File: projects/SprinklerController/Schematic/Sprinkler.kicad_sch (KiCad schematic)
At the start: 37 parts

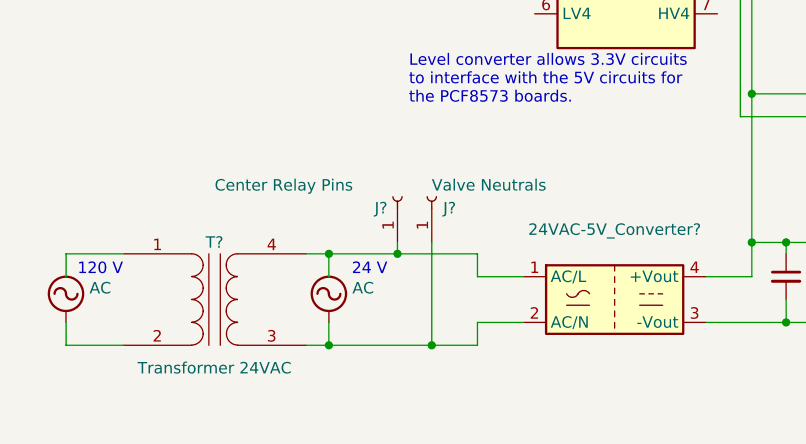
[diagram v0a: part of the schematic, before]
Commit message: Minor correction to schematic
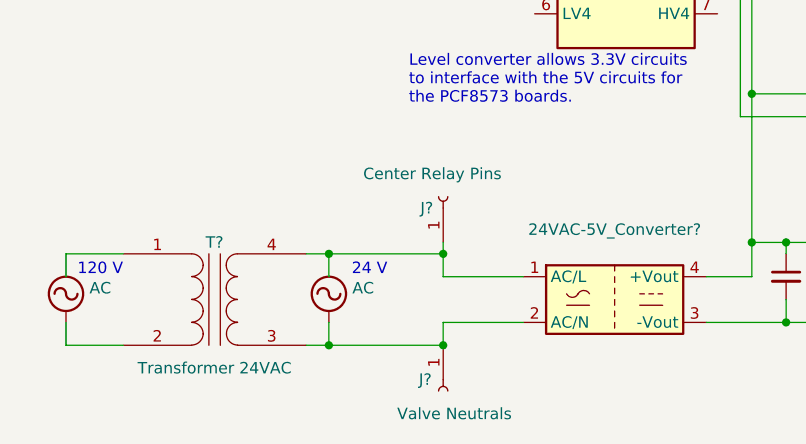
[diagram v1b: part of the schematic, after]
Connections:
- net at U?.3 (P2): no longer U?.3 (P2)
- net at U?.4 (VCC): no longer U?.4 (VCC)
- net at U?.1 (SCL): now also U?.1 (SCL)
- net at U?.1 (SCL): no longer U?.1 (SCL)
- net at U?.2 (SDA): now also U?.2 (SDA)
- net at U?.2 (SDA): no longer U?.2 (SDA)
- net at U?.3 (P2): now also U?.3 (P2)
- net at U?.4 (VCC): now also U?.4 (VCC)
- new net: U?.3 (P2), U?.3 (P2)
- new net: U?.4 (VCC), U?.4 (VCC)
- now unconnected: U?.3 (P2), U?.4 (VCC)
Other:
- moved on the sheet: J?
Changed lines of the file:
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@@
   (junction (at 246.38 104.14) (diameter 0) (color 0 0 0 0)
   )
+  (junction (at 66.04 184.15) (diameter 0) (color 0 0 0 0)
+  )
   (junction (at 166.37 104.14) (diameter 0) (color 0 0 0 0)
   )
@@
   (junction (at 199.39 59.69) (diameter 0) (color 0 0 0 0)
   )
-  (junction (at 60.96 173.99) (diameter 0) (color 0 0 0 0)
-  )
   (junction (at 54.61 137.16) (diameter 0) (color 0 0 0 0)
   )
@@
   (junction (at 240.03 129.54) (diameter 0) (color 0 0 0 0)
   )
-  (junction (at 64.77 184.15) (diameter 0) (color 0 0 0 0)
+  (junction (at 66.04 173.99) (diameter 0) (color 0 0 0 0)
   )
   (junction (at 246.38 92.71) (diameter 0) (color 0 0 0 0)
@@
     (stroke (width 0) (type default) (color 0 0 0 0))
   )
-  (wire (pts (xy 64.77 184.15) (xy 69.85 184.15))
+  (wire (pts (xy 53.34 184.15) (xy 66.04 184.15))
     (stroke (width 0) (type default) (color 0 0 0 0))
   )
@@
     (stroke (width 0) (type default) (color 0 0 0 0))
   )
-  (wire (pts (xy 69.85 184.15) (xy 69.85 181.61))
-    (stroke (width 0) (type default) (color 0 0 0 0))
-  )
-  (wire (pts (xy 60.96 173.99) (xy 69.85 173.99))
-    (stroke (width 0) (type default) (color 0 0 0 0))
-  )
   (wire (pts (xy 157.48 100.33) (xy 180.34 100.33))
     (stroke (width 0) (type default) (color 0 0 0 0))
@@
     (stroke (width 0) (type default) (color 0 0 0 0))
   )
+  (wire (pts (xy 74.93 176.53) (xy 66.04 176.53))
+    (stroke (width 0) (type default) (color 0 0 0 0))
+  )
   (wire (pts (xy 204.47 134.62) (xy 198.12 134.62))
     (stroke (width 0) (type default) (color 0 0 0 0))
@@
     (stroke (width 0) (type default) (color 0 0 0 0))
   )
+  (wire (pts (xy 66.04 181.61) (xy 66.04 184.15))
+    (stroke (width 0) (type default) (color 0 0 0 0))
+  )
   (wire (pts (xy 207.01 92.71) (xy 207.01 104.14))
     (stroke (width 0) (type default) (color 0 0 0 0))
@@
     (stroke (width 0) (type default) (color 0 0 0 0))
   )
+  (wire (pts (xy 66.04 172.72) (xy 66.04 173.99))
+    (stroke (width 0) (type default) (color 0 0 0 0))
+  )
   (wire (pts (xy 279.4 46.99) (xy 279.4 59.69))
     (stroke (width 0) (type default) (color 0 0 0 0))
@@
     (stroke (width 0) (type default) (color 0 0 0 0))
   )
-  (wire (pts (xy 60.96 172.72) (xy 60.96 173.99))
-    (stroke (width 0) (type default) (color 0 0 0 0))
-  )
   (wire (pts (xy 279.4 72.39) (xy 279.4 83.82))
     (stroke (width 0) (type default) (color 0 0 0 0))
@@
     (stroke (width 0) (type default) (color 0 0 0 0))
   )
-  (wire (pts (xy 69.85 176.53) (xy 74.93 176.53))
-    (stroke (width 0) (type default) (color 0 0 0 0))
-  )
   (wire (pts (xy 53.34 173.99) (xy 53.34 176.53))
     (stroke (width 0) (type default) (color 0 0 0 0))
@@
     (stroke (width 0) (type default) (color 0 0 0 0))
   )
+  (wire (pts (xy 66.04 176.53) (xy 66.04 173.99))
+    (stroke (width 0) (type default) (color 0 0 0 0))
+  )
   (wire (pts (xy 158.75 111.76) (xy 180.34 111.76))
     (stroke (width 0) (type default) (color 0 0 0 0))
@@
     (stroke (width 0) (type default) (color 0 0 0 0))
   )
-  (wire (pts (xy 53.34 184.15) (xy 64.77 184.15))
-    (stroke (width 0) (type default) (color 0 0 0 0))
-  )
   (wire (pts (xy 34.29 34.29) (xy 34.29 63.5))
     (stroke (width 0) (type default) (color 0 0 0 0))
@@
     (stroke (width 0) (type default) (color 0 0 0 0))
   )
-  (wire (pts (xy 69.85 173.99) (xy 69.85 176.53))
-    (stroke (width 0) (type default) (color 0 0 0 0))
-  )
   (wire (pts (xy 160.02 123.19) (xy 180.34 123.19))
     (stroke (width 0) (type default) (color 0 0 0 0))
@@
     (stroke (width 0) (type default) (color 0 0 0 0))
   )
-  (wire (pts (xy 69.85 181.61) (xy 74.93 181.61))
-    (stroke (width 0) (type default) (color 0 0 0 0))
-  )
   (wire (pts (xy 199.39 72.39) (xy 199.39 83.82))
     (stroke (width 0) (type default) (color 0 0 0 0))
@@
     (stroke (width 0) (type default) (color 0 0 0 0))
   )
-  (wire (pts (xy 64.77 172.72) (xy 64.77 184.15))
-    (stroke (width 0) (type default) (color 0 0 0 0))
-  )
   (wire (pts (xy 180.34 104.14) (xy 166.37 104.14))
     (stroke (width 0) (type default) (color 0 0 0 0))
@@
     (stroke (width 0) (type default) (color 0 0 0 0))
   )
-  (wire (pts (xy 53.34 173.99) (xy 60.96 173.99))
+  (wire (pts (xy 53.34 173.99) (xy 66.04 173.99))
     (stroke (width 0) (type default) (color 0 0 0 0))
   )
@@
   )
   (wire (pts (xy 24.13 184.15) (xy 30.48 184.15))
+    (stroke (width 0) (type default) (color 0 0 0 0))
+  )
+  (wire (pts (xy 74.93 181.61) (xy 66.04 181.61))
     (stroke (width 0) (type default) (color 0 0 0 0))
   )
@@
     (pin "5")
   )
-  (symbol (lib_id "Connector:Conn_01x01_Female") (at 60.96 167.64 90) (unit 1)
+  (symbol (lib_id "Connector:Conn_01x01_Female") (at 66.04 167.64 90) (unit 1)
     (in_bom yes) (on_board yes)
-    (property "Reference" "J?" (id 0) (at 58.42 168.91 90)
+    (property "Reference" "J?" (id 0) (at 63.5 168.91 90)
       (effects (font (size 1.27 1.27)) (justify right))
     )
-    (property "Value" "Center Relay Pins" (id 1) (at 40.64 166.37 90)
+    (property "Value" "Center Relay Pins" (id 1) (at 57.15 165.1 90)
       (effects (font (size 1.27 1.27)) (justify right))
     )
-    (property "Footprint" "" (id 2) (at 60.96 167.64 0)
-      (effects (font (size 1.27 1.27)) hide)
-    )
-    (property "Datasheet" "~" (id 3) (at 60.96 167.64 0)
+    (property "Footprint" "" (id 2) (at 66.04 167.64 0)
+      (effects (font (size 1.27 1.27)) hide)
+    )
+    (property "Datasheet" "~" (id 3) (at 66.04 167.64 0)
       (effects (font (size 1.27 1.27)) hide)
     )
@@
     (pin "9")
   )
-  (symbol (lib_id "Connector:Conn_01x01_Female") (at 64.77 167.64 90) (unit 1)
+  (symbol (lib_id "Connector:Conn_01x01_Female") (at 66.04 189.23 270) (unit 1)
     (in_bom yes) (on_board yes)
-    (property "Reference" "J?" (id 0) (at 66.04 168.91 90)
+    (property "Reference" "J?" (id 0) (at 64.77 187.96 90)
       (effects (font (size 1.27 1.27)) (justify right))
     )
-    (property "Value" "Valve Neutrals" (id 1) (at 64.77 166.37 90)
+    (property "Value" "Valve Neutrals" (id 1) (at 73.66 191.77 90)
       (effects (font (size 1.27 1.27)) (justify right))
     )
-    (property "Footprint" "" (id 2) (at 64.77 167.64 0)
-      (effects (font (size 1.27 1.27)) hide)
-    )
-    (property "Datasheet" "~" (id 3) (at 64.77 167.64 0)
-      (effects (font (size 1.27 1.27)) hide)
-    )
+    (property "Footprint" "" (id 2) (at 66.04 189.23 0)
+      (effects (font (size 1.27 1.27)) hide)
+    )
+    (property "Datasheet" "~" (id 3) (at 66.04 189.23 0)
+      (effects (font (size 1.27 1.27)) hide)
+    )
